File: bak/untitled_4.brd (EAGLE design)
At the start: 100 x 93.2 mm, 98 parts, among them IC1 LM1875T, IC2 LM1875T, IC3 LM1875T, IC4 LM1875T, IC5 NE5532N, IC6 NE5532N, J2 power, J3 audio_output, J4 B3P-VH(LF)(SN), J5 +25v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

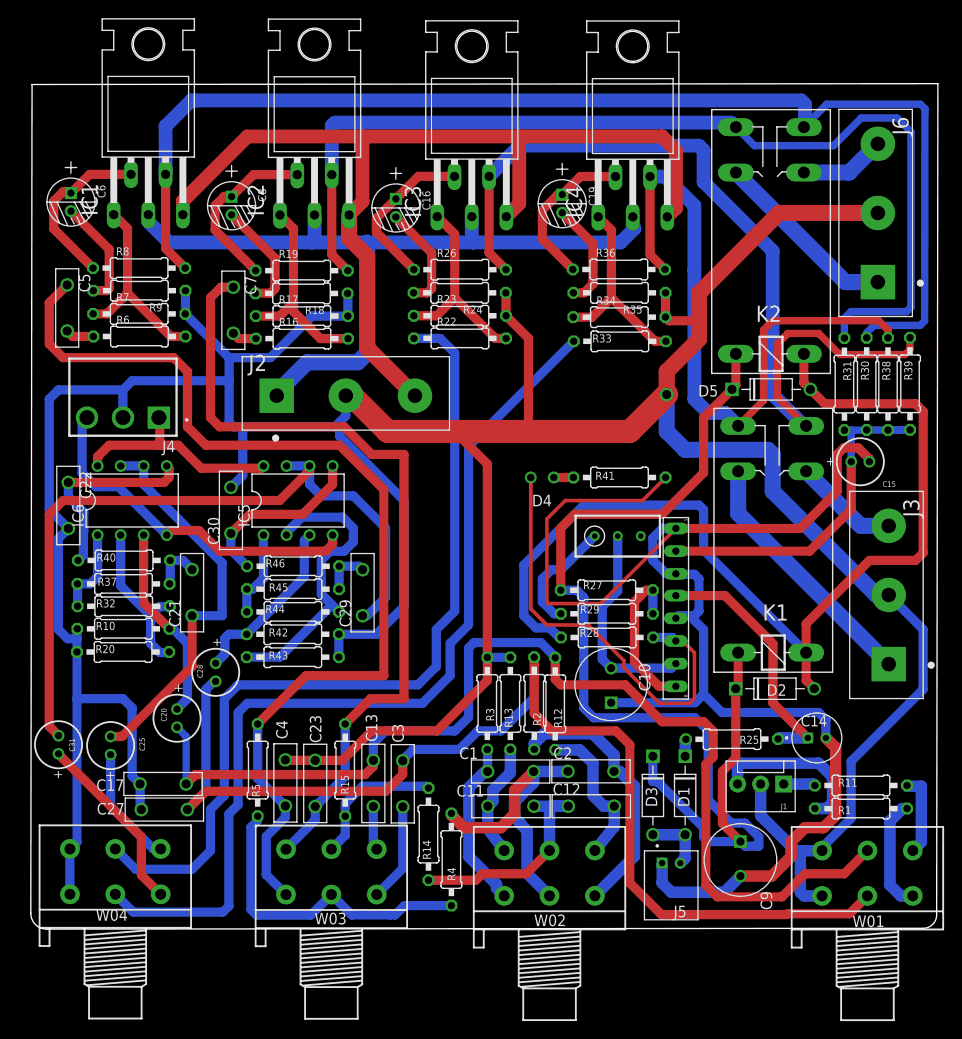
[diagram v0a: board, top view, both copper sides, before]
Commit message: 后级放大:更新
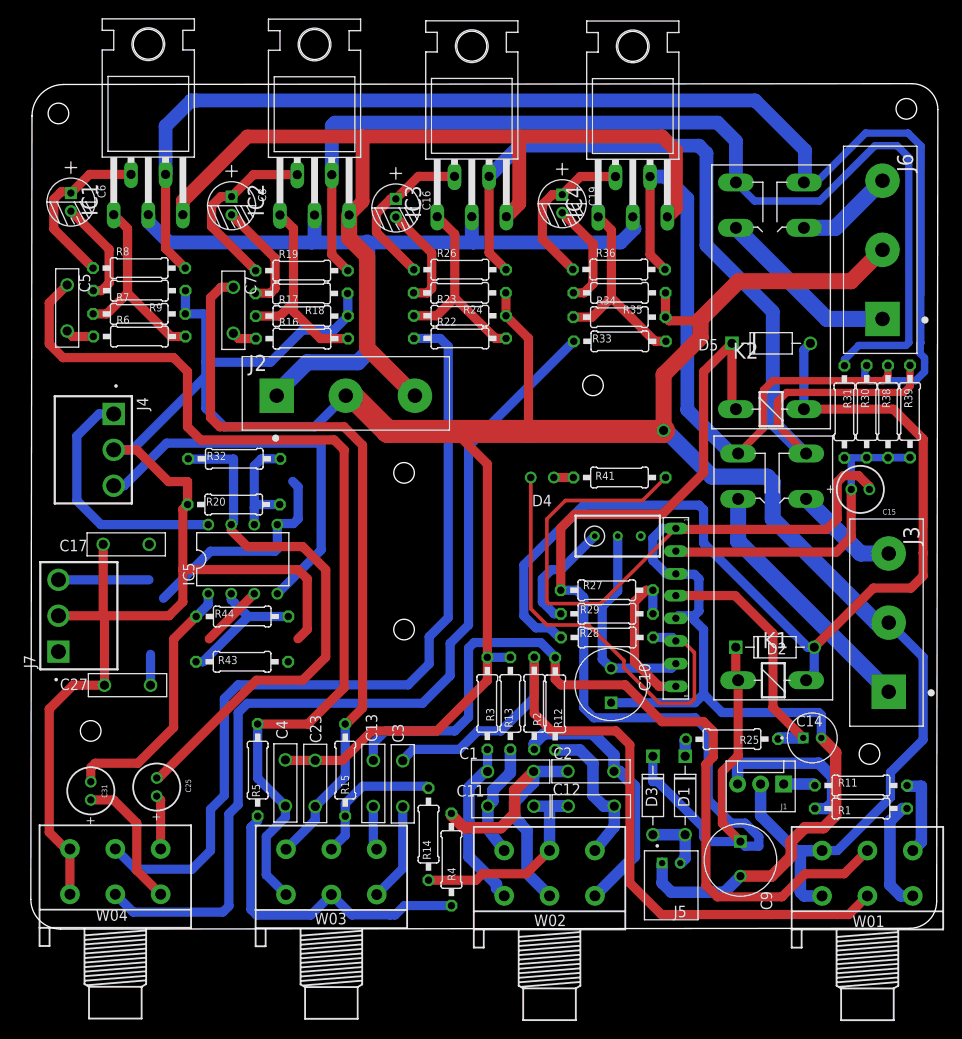
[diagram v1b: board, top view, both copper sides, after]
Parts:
- removed C20, C28: 10µF/50v, Wurth_Capacitors_WCAP-AT1H:WCAP-AT1H_5X11(DXL)
- removed C21, C29: 0.22, Audio-Power-amlifier:5.08MM-独石电容
- removed C22, C30: 104, Audio-Power-amlifier:5.08MM-独石电容
- removed IC6: NE5532N, linear:DIL08
- removed R10, R42: 47k, OPL_Resistor:PR-D2.3XL6.5MM
- removed R37, R40, R45, R46: 10k, OPL_Resistor:PR-D2.3XL6.5MM
- added J7: B3P-VH(LF)(SN), Connectors:HDR-03
- moved C17 26.7 mm to (10.5, 42.4)
- moved R20 20.3 mm to (22.2, 46.8)
- moved R32 20.3 mm to (22.3, 51.8)
- moved C27 14.3 mm to (10.7, 26.9)
- moved IC5 8.89 mm to (23.4, 40.8)
- moved C25 6.83 mm to (13.9, 15.7)
- moved C31 6.20 mm to (6.62, 15.2)
- moved K2 6.10 mm to (81.5, 59.9)
- moved R43 5.61 mm to (23.4, 29.5)
- moved R44 5.61 mm to (23.2, 34.5)
- moved D5 5.08 mm to (81.6, 64.6)
- moved D2 4.57 mm to (82.0, 31.1)
- moved J6 4.10 mm to (93.9, 74.9)
- moved J4 3.70 mm to (9.14, 52.8), turned to 270 degrees
- moved C15 3.05 mm to (91.4, 48.5)
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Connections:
- removed net N$27: C20.1, IC6.3, R10.2
- removed net N$49: C28.1, IC5.3, R42.2
- removed net N$59: C21.P$2, R37.1, R40.2
- removed net N$60: C22.P$1, IC6.5, R40.1
- removed net N$61: C21.P$1, C25.2, IC6.6, IC6.7
- removed net N$62: C29.P$1, C31.2, IC5.6, IC5.7
- removed net N$65: C29.P$2, R45.1, R46.2
- removed net N$66: C30.P$1, IC5.5, R46.1
- new net N$13: C17.P$2, IC5.5, J7.3
- new net N$53: C3.P$1, R2.1, W01.1-2
- net GND: now also J7.2; no longer C22.P$2, C30.P$2, R10.1, R42.1
- net N$16: now also IC5.3, J7.1; no longer C28.2, C3.P$1, R2.1, W01.1-2
- net N$39: now also IC5.6; no longer IC6.2
- net N$55: now also C25.2, IC5.7; no longer IC6.1, R37.2
- net N$58: no longer C17.P$2, C20.2
- net N$64: now also C31.2; no longer R45.2
- net V+: no longer IC6.8
- net V-: no longer IC6.4
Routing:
- net N$16: track 126.2 -> 10.8 mm
- net N$53: track 0.00 -> 83.8 mm
- net N$62: track 82.0 -> 0.00 mm
- net N$55: track 9.60 -> 59.0 mm
- net N$61: track 43.7 -> 0.00 mm
- net N$13: track 0.00 -> 34.4 mm
- net N$58: track 120.4 -> 91.7 mm
- net GND: track 439.3 -> 411.9 mm
- net N$60: track 22.3 -> 0.00 mm
- net N$27: track 21.9 -> 0.00 mm
- net N$66: track 19.8 -> 0.00 mm
- net N$49: track 19.6 -> 0.00 mm
- net N$64: track 9.59 -> 28.8 mm
- net N$63: track 33.0 -> 15.5 mm
- net N$43: track 125.8 -> 135.0 mm
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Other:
- outline, holes or cut-outs redrawn
